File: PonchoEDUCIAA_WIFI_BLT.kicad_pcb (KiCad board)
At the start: 2 copper layers, 57.5 x 59.5 mm, 25 parts, among them J1 UART, SW1 Reset, SW2 Boot, U1 ESP32-WROOM

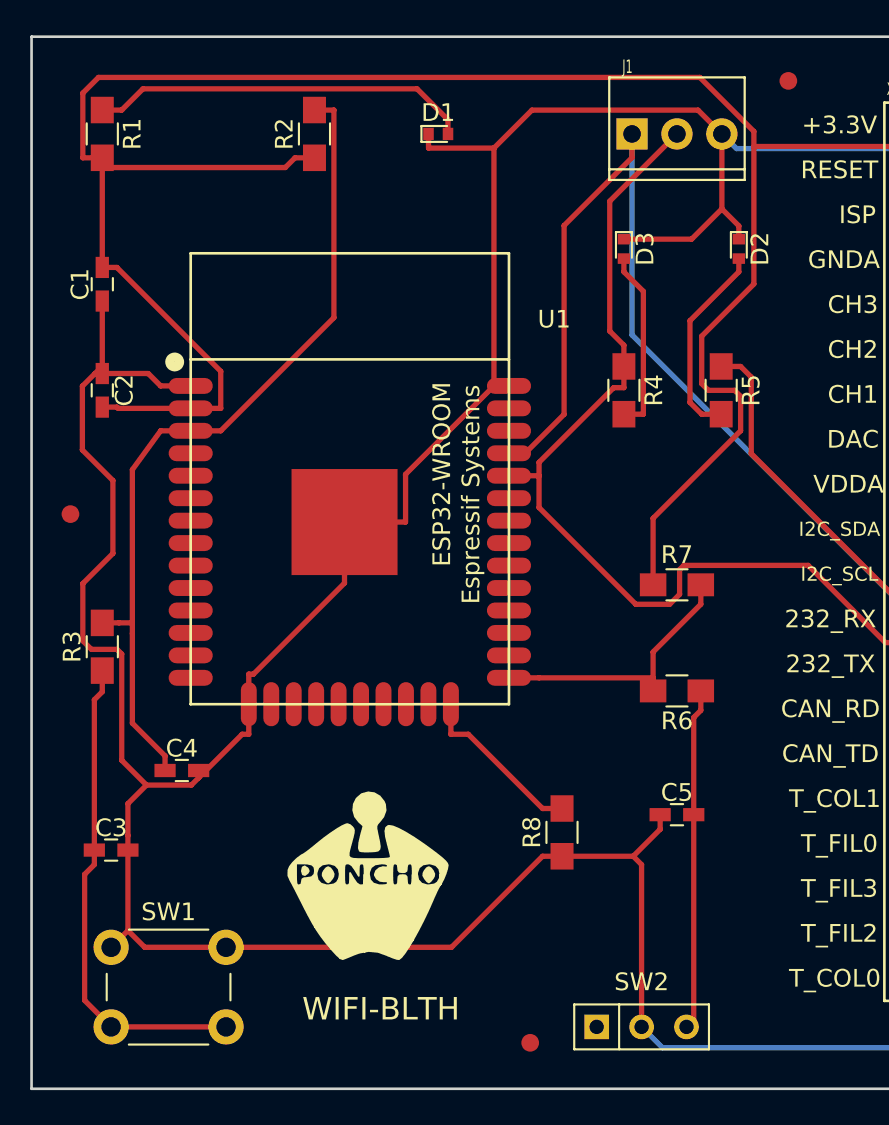
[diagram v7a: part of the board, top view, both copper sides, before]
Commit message: Se corrigen detalles en el pcb y se generan imagenes de la vista 3d
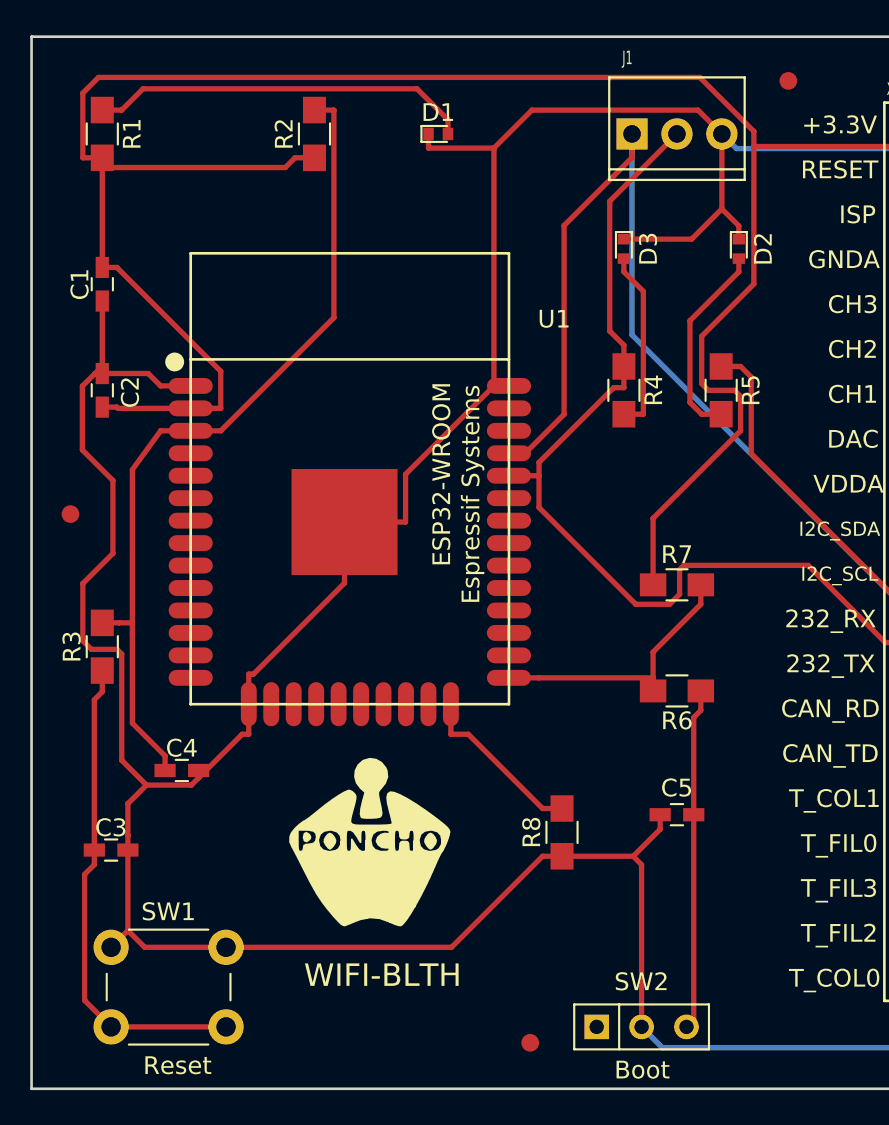
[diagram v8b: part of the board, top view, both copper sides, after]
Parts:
- moved G1 1.90 mm to (148.1, 119.6)
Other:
- rule trace_min: 0.25 -> 0.3
- board text added: "Boot"
- board text added: "Reset"
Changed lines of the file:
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@@
     (area 128.924999 73.924999 186.575001 133.575001)
     (thickness 1.6)
-    (drawings 4)
+    (drawings 6)
     (tracks 195)
     (zones 0)
@@
     (zone_clearance 0.3)
     (zone_45_only no)
-    (trace_min 0.25)
+    (trace_min 0.3)
     (segment_width 0.2)
     (edge_width 0.15)
@@
     (tags "capacitor 0603")
     (attr smd)
-    (fp_text reference C2 (at 0 -1.25 270) (layer F.SilkS)
+    (fp_text reference C2 (at 0.1 -1.6 270) (layer F.SilkS)
       (effects (font (size 1 1) (thickness 0.15)))
     )
@@
       (effects (font (size 1 1) (thickness 0.15)))
     )
-    (fp_text user %R (at 0 -1.25 270) (layer F.Fab)
+    (fp_text user %R (at 0.1 -1.6 270) (layer F.Fab)
       (effects (font (size 1 1) (thickness 0.15)))
     )
@@
     (tags "capacitor 0603")
     (attr smd)
-    (fp_text reference C5 (at 0 -1.25) (layer F.SilkS)
+    (fp_text reference C5 (at 0 -1.5) (layer F.SilkS)
       (effects (font (size 1 1) (thickness 0.15)))
     )
@@
       (effects (font (size 1 1) (thickness 0.15)))
     )
-    (fp_text user %R (at 0 -1.25) (layer F.Fab)
+    (fp_text user %R (at 0 -1.5) (layer F.Fab)
       (effects (font (size 1 1) (thickness 0.15)))
     )
@@
     (tags "LED led 0402 SMD smd SMT smt smdled SMDLED smtled SMTLED")
     (attr smd)
-    (fp_text reference D2 (at 0 -1.2 270) (layer F.SilkS)
+    (fp_text reference D2 (at 0 -1.4 270) (layer F.SilkS)
       (effects (font (size 1 1) (thickness 0.15)))
     )
@@
     (tags "LED led 0402 SMD smd SMT smt smdled SMDLED smtled SMTLED")
     (attr smd)
-    (fp_text reference D3 (at 0 -1.2 270) (layer F.SilkS)
+    (fp_text reference D3 (at 0 -1.4 270) (layer F.SilkS)
       (effects (font (size 1 1) (thickness 0.15)))
     )
@@
   (module PonchoEDUCIAA_WIFI_BLTH:CON_PALETA_3 (layer TOP)
     (at 165.5 79.5)
-    (fp_text reference J1 (at -2.8 -3.8) (layer F.SilkS)
+    (fp_text reference J1 (at -2.8 -4.3) (layer F.SilkS)
       (effects (font (size 0.762 0.4572) (thickness 0.127)))
     )
@@
   )
   (module PonchoEDUCIAA_WIFI_BLTH:Logo_Poncho (layer TOP)
-    (at 148 121.5)
+    (at 148.1 119.6)
     (fp_text reference G1 (at 0.127 5.588) (layer F.SilkS) hide
       (effects (font (thickness 0.3)))
@@
     )
   )
+  (gr_text Boot (at 163.53 132.45) (layer F.SilkS)
+    (effects (font (size 1 1) (thickness 0.15)))
+  )
+  (gr_text Reset (at 137.25 132.2) (layer F.SilkS)
+    (effects (font (size 1 1) (thickness 0.15)))
+  )
   (gr_line (start 129 133.5) (end 129 74) (angle 90) (layer Edge.Cuts) (width 0.15))
